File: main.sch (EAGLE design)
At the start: 38 parts, among them IC1 ATTINY13A-SSH, IC2 TP4056-42-ESOP8, IC3 LM27313XMFX_NOPB, IC4 TPL5110DDCT, T1A 2N4401, T1B NPN, X1 MINI-USB-UX60A-MB-5ST, X2 332-02

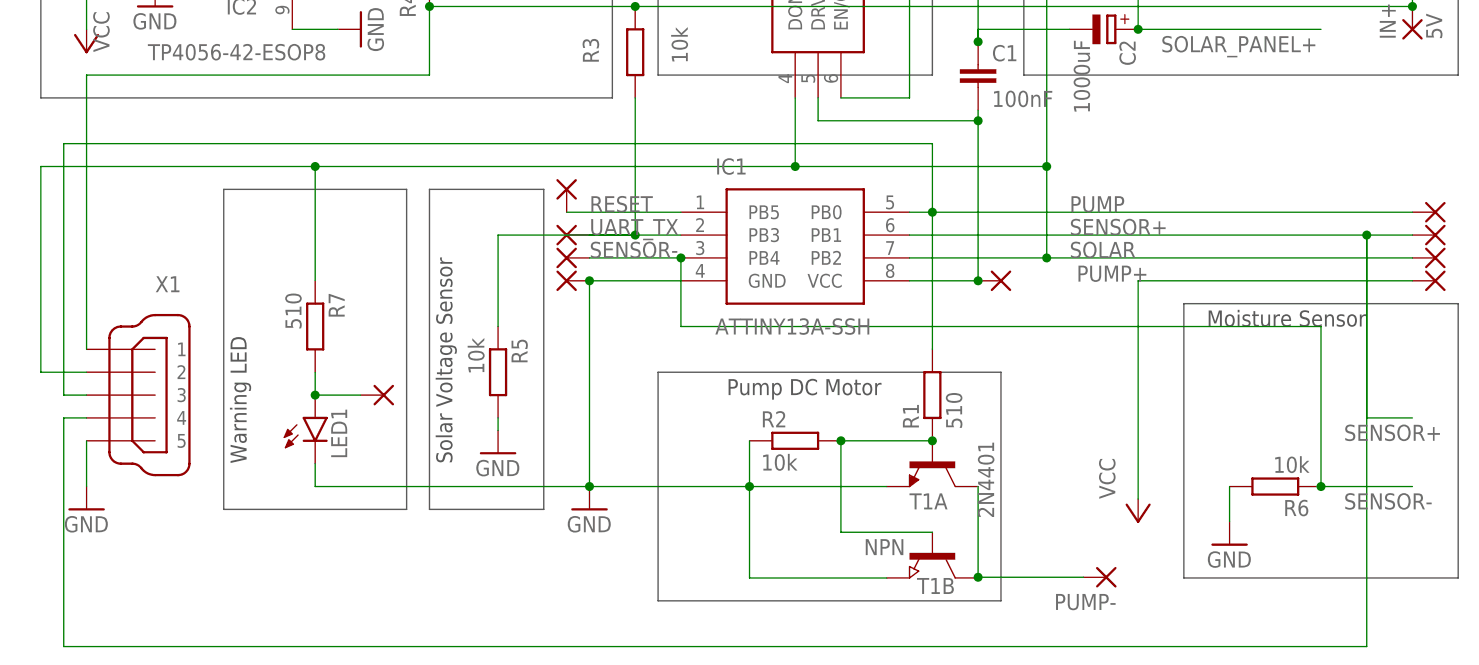
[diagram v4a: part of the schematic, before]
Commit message: remapped LED gpio
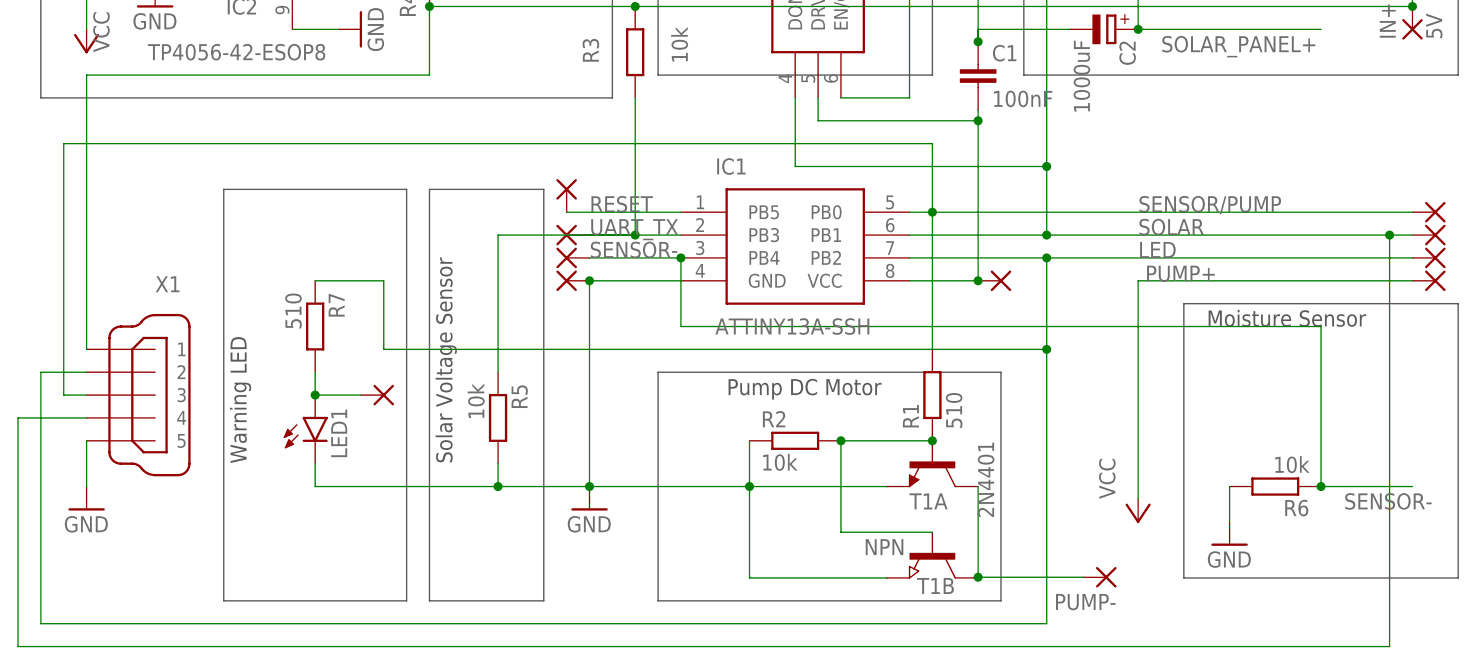
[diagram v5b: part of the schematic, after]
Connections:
- net PUMP renamed SENSOR/PUMP
- removed net SENSOR+: IC1.PB1, PAD6.P, X1.4
- new net LED: IC1.PB2, PAD4.P, R7.1, X1.2
- net SOLAR: now also IC1.PB1, PAD6.P, X1.4; no longer IC1.PB2, PAD4.P, R7.1, X1.2
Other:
- moved on the sheet: R5
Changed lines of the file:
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@@
 <part name="GND1" library="supply1" library_urn="urn:adsk.eagle:library:371" deviceset="GND" device=""/>
 <part name="R5" library="resistor" library_urn="urn:adsk.eagle:library:348" deviceset="R-EU_" device="M0805" package3d_urn="urn:adsk.eagle:package:23556/1" value="10k"/>
-<part name="GND9" library="supply1" library_urn="urn:adsk.eagle:library:371" deviceset="GND" device=""/>
 <part name="X2" library="con-garry" library_urn="urn:adsk.eagle:library:147" deviceset="332-02" device="" package3d_urn="urn:adsk.eagle:package:6810/1"/>
 <part name="GND10" library="supply1" library_urn="urn:adsk.eagle:library:371" deviceset="GND" device=""/>
@@
 <wire x1="137.16" y1="119.38" x2="88.9" y2="119.38" width="0.1524" layer="97"/>
 <text x="91.44" y="116.84" size="1.778" layer="97">Solar Charger</text>
-<wire x1="20.32" y1="60.96" x2="20.32" y2="25.4" width="0.1524" layer="97"/>
-<wire x1="20.32" y1="25.4" x2="0" y2="25.4" width="0.1524" layer="97"/>
-<wire x1="0" y1="25.4" x2="0" y2="60.96" width="0.1524" layer="97"/>
+<wire x1="20.32" y1="60.96" x2="20.32" y2="15.24" width="0.1524" layer="97"/>
+<wire x1="20.32" y1="15.24" x2="0" y2="15.24" width="0.1524" layer="97"/>
+<wire x1="0" y1="15.24" x2="0" y2="60.96" width="0.1524" layer="97"/>
 <wire x1="0" y1="60.96" x2="20.32" y2="60.96" width="0.1524" layer="97"/>
 <wire x1="48.26" y1="40.64" x2="86.36" y2="40.64" width="0.1524" layer="97"/>
@@
 <wire x1="137.16" y1="48.26" x2="106.68" y2="48.26" width="0.1524" layer="97"/>
 <text x="25.4" y="30.48" size="1.778" layer="97" rot="R90">Solar Voltage Sensor</text>
-<wire x1="35.56" y1="60.96" x2="35.56" y2="25.4" width="0.1524" layer="97"/>
-<wire x1="35.56" y1="25.4" x2="22.86" y2="25.4" width="0.1524" layer="97"/>
+<wire x1="35.56" y1="60.96" x2="35.56" y2="15.24" width="0.1524" layer="97"/>
+<wire x1="35.56" y1="15.24" x2="22.86" y2="15.24" width="0.1524" layer="97"/>
 <wire x1="35.56" y1="60.96" x2="22.86" y2="60.96" width="0.1524" layer="97"/>
-<wire x1="22.86" y1="60.96" x2="22.86" y2="25.4" width="0.1524" layer="97"/>
+<wire x1="22.86" y1="60.96" x2="22.86" y2="15.24" width="0.1524" layer="97"/>
 <text x="50.8" y="83.82" size="1.778" layer="97" rot="R90">Low Power Sleep</text>
 <wire x1="48.26" y1="127" x2="48.26" y2="73.66" width="0.1524" layer="97"/>
@@
 </instance>
 <instance part="PUMP+" gate="1" x="134.62" y="50.8" smashed="yes" rot="R180">
-<attribute name="NAME" x="102.743" y="52.4858" size="1.778" layer="95" rot="R180"/>
+<attribute name="NAME" x="110.363" y="52.4858" size="1.778" layer="95" rot="R180"/>
 <attribute name="VALUE" x="135.763" y="54.102" size="1.778" layer="96" rot="R180"/>
 </instance>
@@
 <attribute name="VALUE" x="129.54" y="101.6" size="1.778" layer="96" rot="R90"/>
 </instance>
-<instance part="R5" gate="G$1" x="30.48" y="40.64" smashed="yes" rot="R270">
-<attribute name="NAME" x="31.9786" y="44.45" size="1.778" layer="95" rot="R270"/>
-<attribute name="VALUE" x="27.178" y="44.45" size="1.778" layer="96" rot="R270"/>
-</instance>
-<instance part="GND9" gate="1" x="30.48" y="31.64" smashed="yes">
-<attribute name="VALUE" x="27.94" y="29.1" size="1.778" layer="96"/>
+<instance part="R5" gate="G$1" x="30.48" y="35.56" smashed="yes" rot="R270">
+<attribute name="NAME" x="31.9786" y="39.37" size="1.778" layer="95" rot="R270"/>
+<attribute name="VALUE" x="27.178" y="39.37" size="1.778" layer="96" rot="R270"/>
 </instance>
 <instance part="X2" gate="-1" x="-12.7" y="111.76" smashed="yes">
@@
 <wire x1="45.72" y1="55.88" x2="40.64" y2="55.88" width="0.1524" layer="91"/>
 <pinref part="R5" gate="G$1" pin="1"/>
-<wire x1="30.48" y1="45.72" x2="30.48" y2="55.88" width="0.1524" layer="91"/>
+<wire x1="30.48" y1="40.64" x2="30.48" y2="55.88" width="0.1524" layer="91"/>
 <wire x1="30.48" y1="55.88" x2="45.72" y2="55.88" width="0.1524" layer="91"/>
 <junction x="45.72" y="55.88"/>
@@
 <pinref part="GND3" gate="1" pin="GND"/>
 <pinref part="LED1" gate="G$1" pin="C"/>
-<wire x1="10.16" y1="27.94" x2="40.64" y2="27.94" width="0.1524" layer="91"/>
+<wire x1="10.16" y1="27.94" x2="30.48" y2="27.94" width="0.1524" layer="91"/>
+<wire x1="30.48" y1="27.94" x2="40.64" y2="27.94" width="0.1524" layer="91"/>
 <wire x1="10.16" y1="30.48" x2="10.16" y2="27.94" width="0.1524" layer="91"/>
+<pinref part="R5" gate="G$1" pin="2"/>
+<wire x1="30.48" y1="30.48" x2="30.48" y2="27.94" width="0.1524" layer="91"/>
+<junction x="30.48" y="27.94"/>
 </segment>
 <segment>
@@
 <pinref part="GND1" gate="1" pin="GND"/>
 <pinref part="IC3" gate="G$1" pin="GND"/>
-</segment>
-<segment>
-<pinref part="GND9" gate="1" pin="GND"/>
-<pinref part="R5" gate="G$1" pin="2"/>
-<wire x1="30.48" y1="34.18" x2="30.48" y2="35.56" width="0.1524" layer="91"/>
 </segment>
 <segment>
@@
 <net name="SOLAR" class="0">
 <segment>
-<pinref part="IC1" gate="G$1" pin="PB2"/>
-<pinref part="PAD4" gate="P" pin="P"/>
-<label x="93.98" y="53.34" size="1.778" layer="95"/>
-<wire x1="76.2" y1="53.34" x2="91.44" y2="53.34" width="0.1524" layer="91"/>
 <pinref part="REG1A" gate="A1" pin="GND"/>
-<wire x1="91.44" y1="53.34" x2="132.08" y2="53.34" width="0.1524" layer="91"/>
 <wire x1="111.76" y1="83.82" x2="91.44" y2="83.82" width="0.1524" layer="91"/>
 <wire x1="91.44" y1="83.82" x2="91.44" y2="63.5" width="0.1524" layer="91"/>
-<junction x="91.44" y="53.34"/>
 <pinref part="IC3" gate="G$1" pin="!SHDN"/>
-<wire x1="91.44" y1="63.5" x2="91.44" y2="53.34" width="0.1524" layer="91"/>
 <wire x1="96.52" y1="106.68" x2="91.44" y2="106.68" width="0.1524" layer="91"/>
 <wire x1="91.44" y1="106.68" x2="91.44" y2="83.82" width="0.1524" layer="91"/>
 <junction x="91.44" y="83.82"/>
-<pinref part="R7" gate="G$1" pin="1"/>
-<wire x1="10.16" y1="50.8" x2="10.16" y2="63.5" width="0.1524" layer="91"/>
 <wire x1="91.44" y1="63.5" x2="63.5" y2="63.5" width="0.1524" layer="91"/>
-<junction x="91.44" y="63.5"/>
-<wire x1="63.5" y1="63.5" x2="10.16" y2="63.5" width="0.1524" layer="91"/>
-<wire x1="10.16" y1="63.5" x2="-20.32" y2="63.5" width="0.1524" layer="91"/>
-<junction x="10.16" y="63.5"/>
-<wire x1="-20.32" y1="63.5" x2="-20.32" y2="40.64" width="0.1524" layer="91"/>
-<pinref part="X1" gate="G$1" pin="2"/>
-<wire x1="-20.32" y1="40.64" x2="-15.24" y2="40.64" width="0.1524" layer="91"/>
 <pinref part="IC4" gate="G$1" pin="DONE"/>
 <wire x1="63.5" y1="71.12" x2="63.5" y2="63.5" width="0.1524" layer="91"/>
-<junction x="63.5" y="63.5"/>
-</segment>
-</net>
-<net name="SENSOR+" class="0">
-<segment>
 <pinref part="IC1" gate="G$1" pin="PB1"/>
 <pinref part="PAD6" gate="P" pin="P"/>
-<label x="93.98" y="55.88" size="1.778" layer="95"/>
-<wire x1="76.2" y1="55.88" x2="127" y2="55.88" width="0.1524" layer="91"/>
-<wire x1="127" y1="55.88" x2="132.08" y2="55.88" width="0.1524" layer="91"/>
-<wire x1="127" y1="35.56" x2="132.08" y2="35.56" width="0.1524" layer="91"/>
-<wire x1="127" y1="35.56" x2="127" y2="55.88" width="0.1524" layer="91"/>
-<junction x="127" y="55.88"/>
-<label x="124.46" y="33.02" size="1.778" layer="95"/>
-<wire x1="127" y1="55.88" x2="127" y2="10.16" width="0.1524" layer="91"/>
-<wire x1="127" y1="10.16" x2="-17.78" y2="10.16" width="0.1524" layer="91"/>
+<label x="101.6" y="55.88" size="1.778" layer="95"/>
+<wire x1="76.2" y1="55.88" x2="91.44" y2="55.88" width="0.1524" layer="91"/>
+<wire x1="91.44" y1="55.88" x2="129.54" y2="55.88" width="0.1524" layer="91"/>
+<wire x1="129.54" y1="55.88" x2="132.08" y2="55.88" width="0.1524" layer="91"/>
+<wire x1="91.44" y1="63.5" x2="91.44" y2="55.88" width="0.1524" layer="91"/>
+<junction x="91.44" y="63.5"/>
+<junction x="91.44" y="55.88"/>
 <pinref part="X1" gate="G$1" pin="4"/>
-<wire x1="-17.78" y1="10.16" x2="-17.78" y2="35.56" width="0.1524" layer="91"/>
-<wire x1="-17.78" y1="35.56" x2="-15.24" y2="35.56" width="0.1524" layer="91"/>
+<wire x1="-22.86" y1="35.56" x2="-15.24" y2="35.56" width="0.1524" layer="91"/>
+<wire x1="129.54" y1="10.16" x2="-22.86" y2="10.16" width="0.1524" layer="91"/>
+<wire x1="-22.86" y1="10.16" x2="-22.86" y2="35.56" width="0.1524" layer="91"/>
+<wire x1="129.54" y1="10.16" x2="129.54" y2="55.88" width="0.1524" layer="91"/>
+<junction x="129.54" y="55.88"/>
 </segment>
 </net>
@@
 </segment>
 </net>
-<net name="PUMP" class="0">
+<net name="SENSOR/PUMP" class="0">
 <segment>
 <pinref part="IC1" gate="G$1" pin="PB0"/>
 <pinref part="PAD5" gate="P" pin="P"/>
-<label x="93.98" y="58.42" size="1.778" layer="95"/>
+<label x="101.6" y="58.42" size="1.778" layer="95"/>
 <wire x1="76.2" y1="58.42" x2="78.74" y2="58.42" width="0.1524" layer="91"/>
 <pinref part="R1" gate="G$1" pin="2"/>
@@
 </segment>
 </net>
+<net name="LED" class="0">
+<segment>
+<pinref part="PAD4" gate="P" pin="P"/>
+<pinref part="IC1" gate="G$1" pin="PB2"/>
+<wire x1="76.2" y1="53.34" x2="91.44" y2="53.34" width="0.1524" layer="91"/>
+<label x="101.6" y="53.34" size="1.778" layer="95"/>
+<pinref part="R7" gate="G$1" pin="1"/>
+<wire x1="91.44" y1="53.34" x2="132.08" y2="53.34" width="0.1524" layer="91"/>
+<wire x1="10.16" y1="50.8" x2="17.78" y2="50.8" width="0.1524" layer="91"/>
+<wire x1="17.78" y1="50.8" x2="17.78" y2="43.18" width="0.1524" layer="91"/>
+<wire x1="17.78" y1="43.18" x2="91.44" y2="43.18" width="0.1524" layer="91"/>
+<wire x1="91.44" y1="43.18" x2="91.44" y2="53.34" width="0.1524" layer="91"/>
+<junction x="91.44" y="53.34"/>
+<pinref part="X1" gate="G$1" pin="2"/>
+<wire x1="-20.32" y1="40.64" x2="-15.24" y2="40.64" width="0.1524" layer="91"/>
+<wire x1="-20.32" y1="40.64" x2="-20.32" y2="12.7" width="0.1524" layer="91"/>
+<wire x1="-20.32" y1="12.7" x2="91.44" y2="12.7" width="0.1524" layer="91"/>
+<wire x1="91.44" y1="12.7" x2="91.44" y2="43.18" width="0.1524" layer="91"/>
+<junction x="91.44" y="43.18"/>
+</segment>
+</net>
